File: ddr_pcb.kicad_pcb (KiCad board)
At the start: 2 copper layers, 16 parts, among them J1 Screw_Terminal_01x04, J2 Screw_Terminal_01x04, J3 Screw_Terminal_01x04, J4 Screw_Terminal_01x06, J5 Screw_Terminal_01x04, U1 ProMicro

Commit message: new: Finished WIP
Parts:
- removed R5: R_Small, Resistor_THT:R_Axial_DIN0204_L3.6mm_D1.6mm_P7.62mm_Horizontal
- added 220ohm1: R_Small, Resistor_THT:R_Axial_DIN0204_L3.6mm_D1.6mm_P5.08mm_Horizontal, F.Cu at (121.9, 38.1)
- added A10: R_Small, Resistor_THT:R_Axial_DIN0204_L3.6mm_D1.6mm_P7.62mm_Horizontal, F.Cu at (109.2, 72.4)
- moved A3 48.7 mm to (94.0, 72.4), turned to 270 degrees
- moved A2 42.6 mm to (88.9, 72.4), turned to 270 degrees
- moved A1 40.9 mm to (99.1, 72.4), turned to 270 degrees
- moved A0 37.1 mm to (104.1, 72.4), turned to 270 degrees
- moved A6 28.5 mm to (91.4, 92.7), turned to 90 degrees
- moved A9 25.7 mm to (106.7, 92.7), turned to 90 degrees
- moved A7 24.4 mm to (96.5, 92.7), turned to 90 degrees
- moved A8 23.3 mm to (101.6, 92.7), turned to 90 degrees
- moved J4 20.1 mm to (130.8, 54.6)
- moved J1 19.7 mm to (130.8, 73.7)
- moved J2 19.4 mm to (130.8, 87.6)
- moved J3 19.2 mm to (130.8, 40.6)
- moved J5 19.1 mm to (130.8, 26.7)
- moved C1 7.73 mm to (114.3, 31.8)
- renumbered R6 to A0, R7 to A1, R8 to A2, R9 to A3, R1 to A6, R2 to A7, R3 to A8, R4 to A9
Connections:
- J5 pad 1: Net-(C1-Pad2) -> Net-(J5-Pad1)
- J5 pad 2: Net-(J5-Pad2) -> Net-(220ohm1-Pad1)
- J5 pad 3: Net-(J5-Pad3) -> Net-(C1-Pad2)
- U1 pad 16: (no net) -> Net-(220ohm1-Pad2)
- U1 pad 23: Net-(J5-Pad3) -> Net-(J5-Pad1)
- U1 pad 8: Net-(J5-Pad2) -> (no net)
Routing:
- net Net-(A6-Pad1): track 0.00 -> 134.8 mm, vias 0 -> 1
- net Net-(C1-Pad2): track 0.00 -> 130.5 mm
- net Net-(A7-Pad1): track 0.00 -> 122.0 mm, vias 0 -> 1
- net Net-(A0-Pad2): track 0.00 -> 96.1 mm
- net Net-(A8-Pad1): track 0.00 -> 94.5 mm, vias 0 -> 1
- net Net-(A2-Pad1): track 0.00 -> 85.9 mm, vias 0 -> 1
- net Net-(A9-Pad1): track 0.00 -> 76.7 mm, vias 0 -> 1
- net Net-(A3-Pad1): track 0.00 -> 74.3 mm, vias 0 -> 1
- net Net-(A1-Pad1): track 0.00 -> 65.2 mm, vias 0 -> 1
- net Net-(A0-Pad1): track 0.00 -> 55.3 mm, vias 0 -> 1
- net Net-(A10-Pad1): track 0.00 -> 42.3 mm, vias 0 -> 1
- net Net-(J5-Pad1): track 0.00 -> 27.7 mm
- net Net-(220ohm1-Pad2): track 0.00 -> 18.8 mm
- net Net-(220ohm1-Pad1): track 0.00 -> 16.3 mm
- net Net-(C1-Pad1): track 0.00 -> 12.0 mm
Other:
- board text added: "FSR_A0"
- board text added: "FSR_A1"
- board text added: "FSR_A10"
- board text added: "FSR_A2"
- board text added: "FSR_A3"
- board text added: "FSR_A6"
- board text added: "FSR_A7"
- board text added: "FSR_A8"
- board text added: "FSR_A9"
- board text added: "LED_DATA"
- board text added: "LED_GND"
- board text added: "LED_PWR"

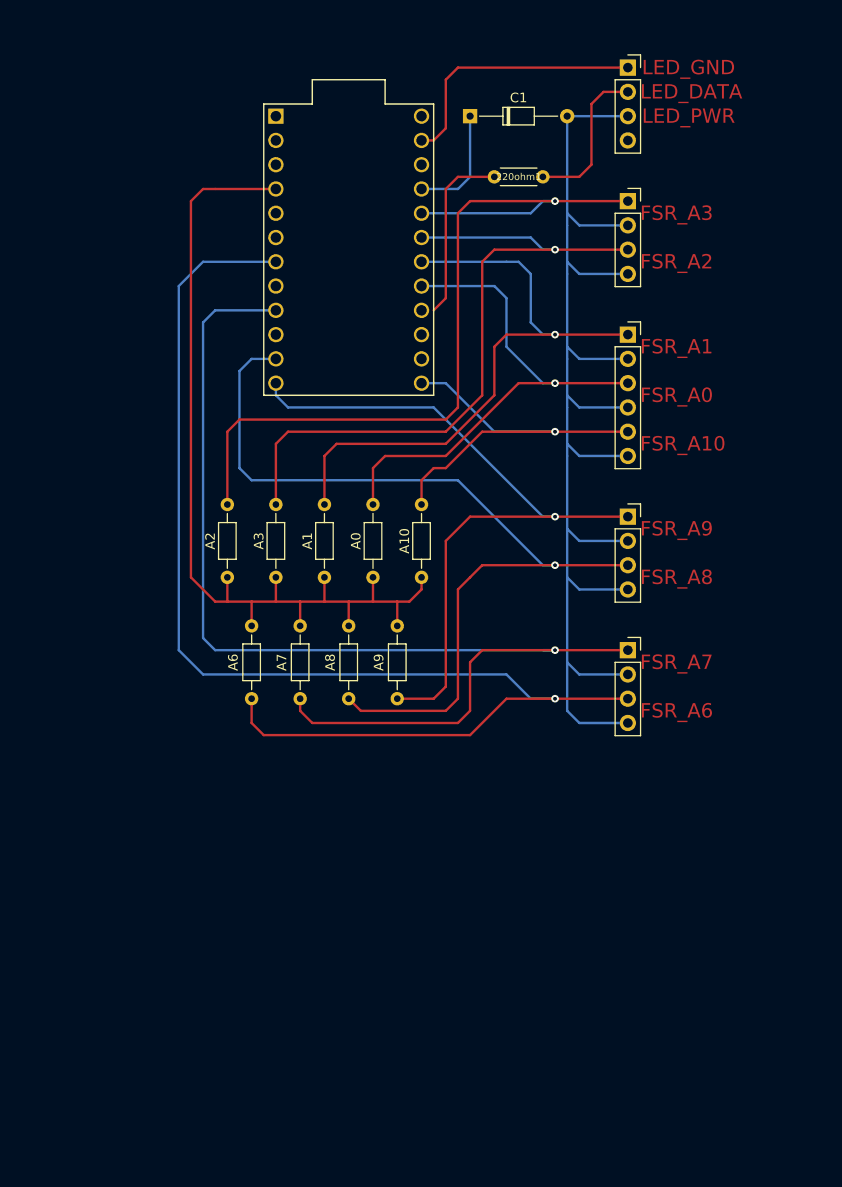
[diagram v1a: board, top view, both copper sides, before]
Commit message: new: Add text to silkscreen
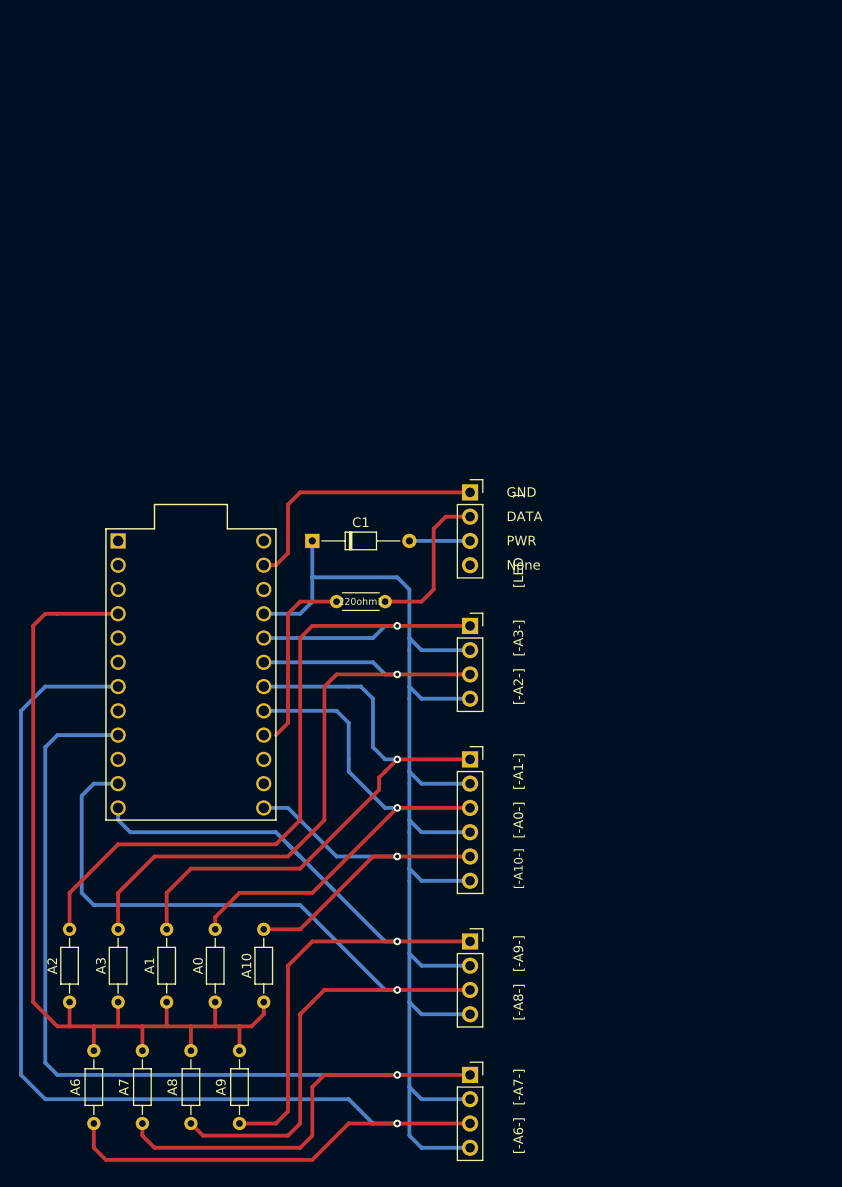
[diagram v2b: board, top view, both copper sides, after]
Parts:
- moved J2 47.4 mm to (114.3, 132.1)
- moved A0 47.4 mm to (87.6, 116.8)
- moved A1 47.4 mm to (82.5, 116.8)
- moved A10 47.4 mm to (92.7, 116.8)
- moved A2 47.4 mm to (72.4, 116.8)
- moved A3 47.4 mm to (77.5, 116.8)
- moved A9 47.4 mm to (90.2, 137.2)
- moved J1 47.4 mm to (114.3, 118.1)
- moved J3 47.4 mm to (114.3, 85.1)
- moved J4 47.4 mm to (114.3, 99.1)
- moved J5 47.4 mm to (114.3, 71.1)
- moved 220ohm1 47.4 mm to (105.4, 82.5)
- moved A6 47.4 mm to (74.9, 137.2)
- moved A7 47.4 mm to (80.0, 137.2)
- moved A8 47.4 mm to (85.1, 137.2)
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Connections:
- J1 pad 2: Net-(C1-Pad2) -> Net-(C1-Pad1)
- J1 pad 4: Net-(C1-Pad2) -> Net-(C1-Pad1)
- J2 pad 2: Net-(C1-Pad2) -> Net-(C1-Pad1)
- J2 pad 4: Net-(C1-Pad2) -> Net-(C1-Pad1)
- J3 pad 2: Net-(C1-Pad2) -> Net-(C1-Pad1)
- J3 pad 4: Net-(C1-Pad2) -> Net-(C1-Pad1)
- J4 pad 2: Net-(C1-Pad2) -> Net-(C1-Pad1)
- J4 pad 4: Net-(C1-Pad2) -> Net-(C1-Pad1)
- J4 pad 6: Net-(C1-Pad2) -> Net-(C1-Pad1)
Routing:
- net Net-(C1-Pad1): track 12.0 -> 141.7 mm
- net Net-(C1-Pad2): track 130.5 -> 6.35 mm
- net Net-(A2-Pad1): track 85.9 -> 82.9 mm
- net Net-(A1-Pad1): track 65.2 -> 62.2 mm
- net Net-(A9-Pad1): track 76.7 -> 78.5 mm
- net Net-(A10-Pad1): track 42.3 -> 40.8 mm
- net Net-(A0-Pad1): track 55.3 -> 53.8 mm
- net Net-(A3-Pad1): track 74.3 -> 72.8 mm
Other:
- net class Default: clearance 0.2 -> 0.127; trace_width 0.25 -> 0.4
- rule trace_clearance: 0.2 -> 0.127
- board text added: "DATA"
- board text added: "GND"
- board text added: "None"
- board text added: "PWR"
- board text added: "[-A0-]"
- board text added: "[-A1-]"
- board text added: "[-A10-]"
- board text added: "[-A2-]"
- board text added: "[-A3-]"
- board text added: "[-A6-]"
- board text added: "[-A7-]"
- board text added: "[-A8-]"
- board text added: "[-A9-]"
- board text added: "[LED ]"
- board text removed: "FSR_A0"
- board text removed: "FSR_A1"
- board text removed: "FSR_A10"
- board text removed: "FSR_A2"
- board text removed: "FSR_A3"
- board text removed: "FSR_A6"
- board text removed: "FSR_A7"
- board text removed: "FSR_A8"
- board text removed: "FSR_A9"
- board text removed: "LED_DATA"
- board text removed: "LED_GND"
- board text removed: "LED_PWR"
